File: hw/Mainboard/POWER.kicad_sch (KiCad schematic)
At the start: 63 parts, among them J10 5V PWR, J11 9V POWER, J18 PET POWER, J7 9V POWER, U10 LM317AG-TN3-R, U13 AMS1117-3.3, U15 LM317AG-TN3-R, U17 LM317AG-TN3-R

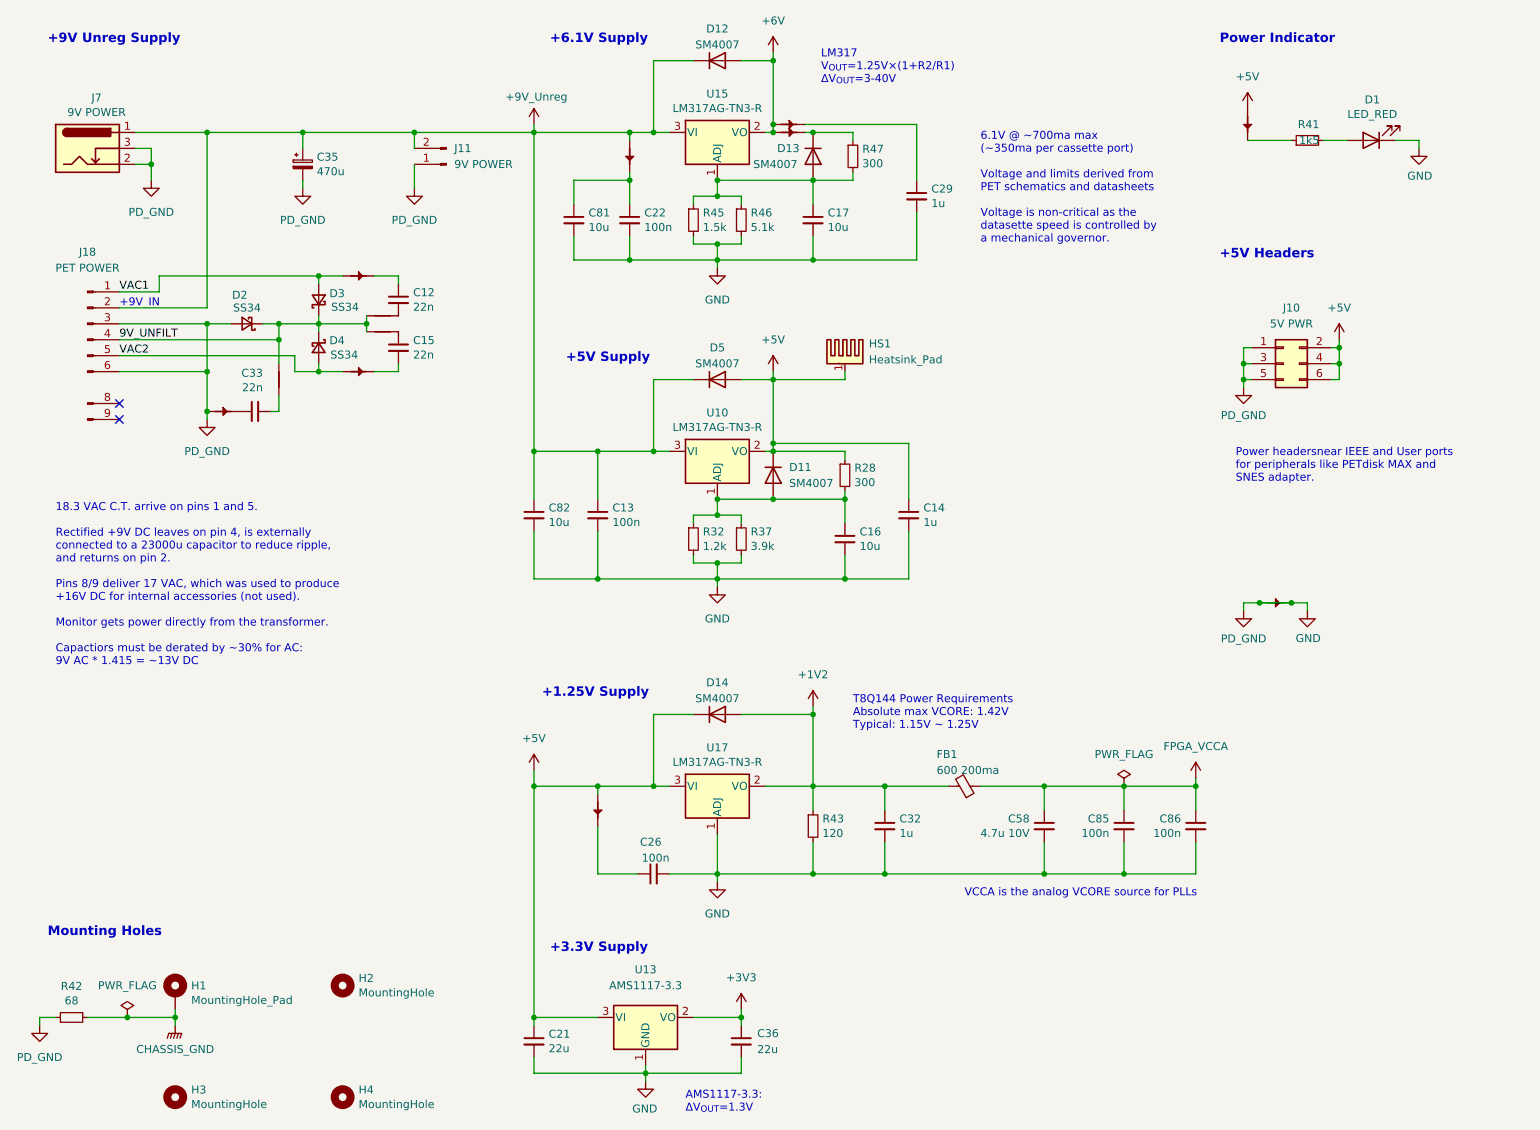
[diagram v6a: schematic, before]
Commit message: hw: 9V DC plug on left edge, change default track size
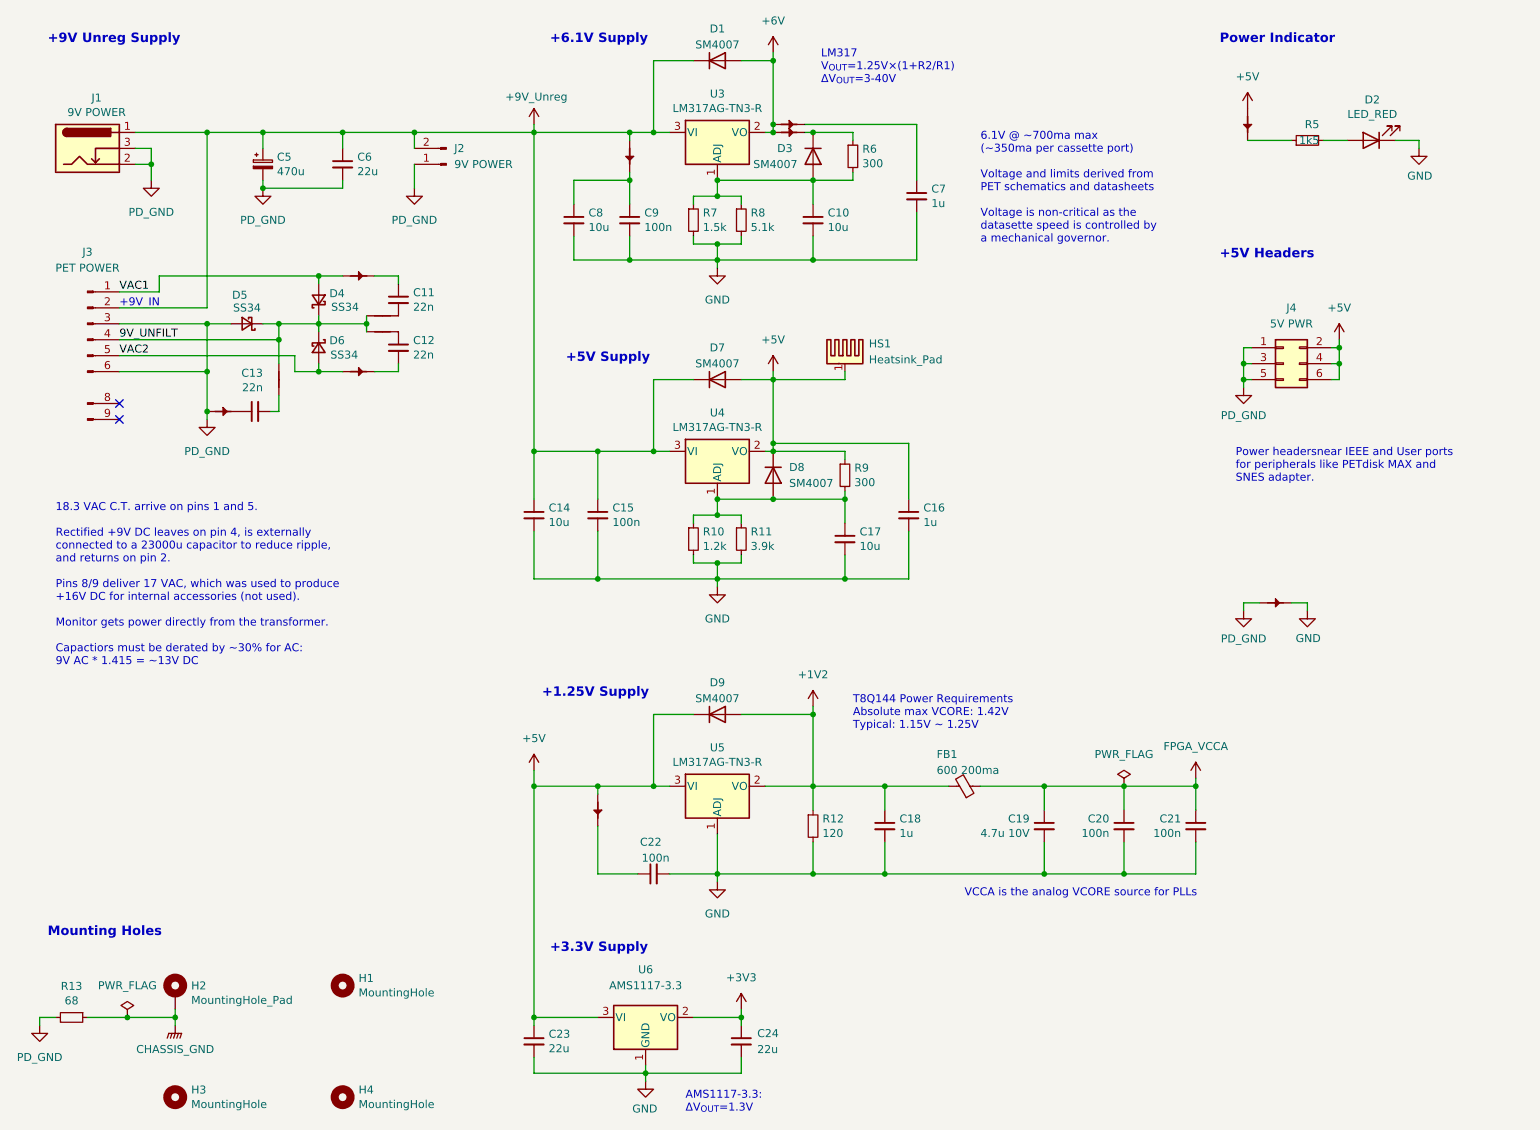
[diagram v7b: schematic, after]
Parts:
- added C6: 22u, Capacitor_SMD:C_0805_2012Metric, symbol Device:C_Small
- renumbered C17 to C10, C12 to C11, C15 to C12, C33 to C13, C82 to C14, C13 to C15, C14 to C16, C16 to C17, C32 to C18, C58 to C19, C85 to C20, C86 to C21, C26 to C22, C21 to C23, C36 to C24, C35 to C5, C29 to C7, C81 to C8, C22 to C9, D12 to D1, D1 to D2, D13 to D3, D3 to D4, D2 to D5, D4 to D6, D5 to D7, D11 to D8, D14 to D9, H2 to H1, H1 to H2, J7 to J1, J11 to J2, J18 to J3, J10 to J4, PT25 to PT1, PT27 to PT10, PT9 to PT11, PT14 to PT12, PT4 to PT2, PT23 to PT3, PT24 to PT4, PT28 to PT5, PT32 to PT6, PT30 to PT7, PT29 to PT8, PT31 to PT9, R32 to R10, R37 to R11, R43 to R12, R42 to R13, R41 to R5, R47 to R6, R45 to R7, R46 to R8, R28 to R9, U15 to U3, U10 to U4, U17 to U5, U13 to U6
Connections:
- net +9V_Unreg: now also C6.1
- net GND: no longer C5.2, D5.2 (A), J1.2, J1.3, J2.1 (Pin_1), J3.3 (GND), J3.6 (GND), J4.1 (Pin_1), J4.3 (Pin_3), J4.5 (Pin_5), PT10.1, PT11.1, R13.2
- new net PD_GND: C5.2, C6.2, D5.2 (A), J1.2, J1.3, J2.1 (Pin_1), J3.3 (GND), J3.6 (GND), J4.1 (Pin_1), J4.3 (Pin_3), J4.5 (Pin_5), PT10.1, PT11.1, R13.2
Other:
- moved on the sheet: C5

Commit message: hw: 2x config switch (wip)
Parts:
- removed C6: 22u, Capacitor_SMD:C_0805_2012Metric, symbol Device:C_Small
- added HS1: Heatsink_Pad, PET:V1100SMDBL, symbol Mechanical:Heatsink_Pad
- renumbered HS1 to HS2
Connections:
- net +6V: now also HS1.1
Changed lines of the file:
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@@
   (junction (at 111.76 107.95) (diameter 0) (color 0 0 0 0)
   )
-  (junction (at 71.12 36.83) (diameter 0) (color 0 0 0 0)
-  )
   (junction (at 49.53 81.28) (diameter 0) (color 0 0 0 0)
   )
@@
   )
   (junction (at 157.48 140.97) (diameter 0) (color 0 0 0 0)
-  )
-  (junction (at 58.42 45.72) (diameter 0) (color 0 0 0 0)
   )
   (junction (at 116.84 36.83) (diameter 0) (color 0 0 0 0)
@@
     (stroke (width 0) (type default) (color 0 0 0 0))
   )
+  (wire (pts (xy 139.7 25.4) (xy 151.13 25.4))
+    (stroke (width 0) (type default) (color 0 0 0 0))
+  )
   (wire (pts (xy 40.64 41.91) (xy 40.64 44.45))
     (stroke (width 0) (type default) (color 0 0 0 0))
@@
     (stroke (width 0) (type default) (color 0 0 0 0))
   )
-  (wire (pts (xy 71.12 44.45) (xy 71.12 45.72))
-    (stroke (width 0) (type default) (color 0 0 0 0))
-  )
   (wire (pts (xy 214.63 71.12) (xy 214.63 73.66))
     (stroke (width 0) (type default) (color 0 0 0 0))
@@
     (stroke (width 0) (type default) (color 0 0 0 0))
   )
-  (wire (pts (xy 58.42 36.83) (xy 71.12 36.83))
-    (stroke (width 0) (type default) (color 0 0 0 0))
-  )
   (wire (pts (xy 144.78 35.56) (xy 162.56 35.56))
     (stroke (width 0) (type default) (color 0 0 0 0))
@@
     (stroke (width 0) (type default) (color 0 0 0 0))
   )
-  (wire (pts (xy 71.12 45.72) (xy 58.42 45.72))
-    (stroke (width 0) (type default) (color 0 0 0 0))
-  )
   (wire (pts (xy 63.5 74.93) (xy 67.31 74.93))
     (stroke (width 0) (type default) (color 0 0 0 0))
@@
     (stroke (width 0) (type default) (color 0 0 0 0))
   )
-  (wire (pts (xy 71.12 36.83) (xy 82.55 36.83))
+  (wire (pts (xy 58.42 36.83) (xy 82.55 36.83))
     (stroke (width 0) (type default) (color 0 0 0 0))
   )
@@
     (stroke (width 0) (type default) (color 0 0 0 0))
   )
-  (wire (pts (xy 71.12 36.83) (xy 71.12 39.37))
-    (stroke (width 0) (type default) (color 0 0 0 0))
-  )
   (wire (pts (xy 116.84 57.15) (xy 107.95 57.15))
     (stroke (width 0) (type default) (color 0 0 0 0))
@@
   )
   (wire (pts (xy 60.96 69.85) (xy 60.96 73.66))
+    (stroke (width 0) (type default) (color 0 0 0 0))
+  )
+  (wire (pts (xy 151.13 25.4) (xy 151.13 24.13))
     (stroke (width 0) (type default) (color 0 0 0 0))
   )
@@
     (effects (font (size 1.27 1.27)) (justify left bottom))
   )
-  (text "LM317\nV_{OUT}=1.25V×(1+R2/R1)\nΔV_{OUT}=3-40V" (at 147.32 29.21 0)
+  (text "LM317\nV_{OUT}=1.25V×(1+R2/R1)\nΔV_{OUT}=3-40V" (at 172.72 29.21 0)
     (effects (font (size 1.27 1.27)) (justify left bottom))
   )
@@
     (pin "1")
   )
-  (symbol (lib_id "Device:C_Small") (at 71.12 41.91 0) (unit 1)
-    (in_bom yes) (on_board yes)
-    (property "Reference" "C6" (id 0) (at 73.4568 40.7416 0)
-      (effects (font (size 1.27 1.27)) (justify left))
-    )
-    (property "Value" "22u" (id 1) (at 73.4568 43.053 0)
-      (effects (font (size 1.27 1.27)) (justify left))
-    )
-    (property "Footprint" "Capacitor_SMD:C_0805_2012Metric" (id 2) (at 71.12 41.91 0)
-      (effects (font (size 1.27 1.27)) hide)
-    )
-    (property "Datasheet" "https://datasheet.lcsc.com/lcsc/2304140030_Samsung-Electro-Mechanics-CL21A226MAQNNNE_C45783.pdf" (id 3) (at 71.12 41.91 0)
-      (effects (font (size 1.27 1.27)) hide)
-    )
-    (property "LCSC" "C45783" (id 4) (at 71.12 41.91 0)
-      (effects (font (size 1.27 1.27)) hide)
-    )
-    (pin "1")
-    (pin "2")
-  )
   (symbol (lib_id "Device:R_Small") (at 127 101.6 0) (unit 1)
     (in_bom yes) (on_board yes)
@@
     )
     (property "Datasheet" "" (id 3) (at 40.64 44.45 0)
+      (effects (font (size 1.27 1.27)) hide)
+    )
+    (pin "1")
+  )
+  (symbol (lib_id "Mechanical:Heatsink_Pad") (at 151.13 21.59 0) (unit 1)
+    (in_bom yes) (on_board yes) (fields_autoplaced)
+    (property "Reference" "HS1" (id 0) (at 154.94 19.6849 0)
+      (effects (font (size 1.27 1.27)) (justify left))
+    )
+    (property "Value" "Heatsink_Pad" (id 1) (at 154.94 22.2249 0)
+      (effects (font (size 1.27 1.27)) (justify left))
+    )
+    (property "Footprint" "PET:V1100SMDBL" (id 2) (at 151.4348 22.86 0)
+      (effects (font (size 1.27 1.27)) hide)
+    )
+    (property "Datasheet" "http://www.assmann-wsw.com/uploads/datasheets/ASS_0855_HS.pdf" (id 3) (at 151.4348 22.86 0)
+      (effects (font (size 1.27 1.27)) hide)
+    )
+    (property "DIGI-KEY" "AE10775-ND" (id 4) (at 151.13 21.59 0)
+      (effects (font (size 1.27 1.27)) hide)
+    )
+    (property "MPN" "V-1100-SMD/B-L" (id 6) (at 151.13 21.59 0)
       (effects (font (size 1.27 1.27)) hide)
     )
@@
   (symbol (lib_id "Mechanical:Heatsink_Pad") (at 151.13 72.39 0) (unit 1)
     (in_bom yes) (on_board yes) (fields_autoplaced)
-    (property "Reference" "HS1" (id 0) (at 154.94 70.4849 0)
-      (effects (font (size 1.27 1.27)) (justify left))
-    )
+    (property "Reference" "HS2" (id 0) (at 154.94 70.4849 0)
+      (effects (font (size 1.27 1.27)) (justify left))
+    )
